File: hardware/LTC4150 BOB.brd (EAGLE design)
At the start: 15.2 x 30.5 mm, 23 parts, among them U1 LTC4150

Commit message: Final cleanup for reds
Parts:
- moved FRAME1 2.54 mm to (-22.9, -11.4)
- moved C2 0.32 mm to (4.45, 14.0)
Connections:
- net VCC renamed VIO
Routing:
- net GND: vias 7 -> 9
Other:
- board text added: "V10"
- board text added: "VIO"
- board text removed: "V02"
- board text removed: "VCC"

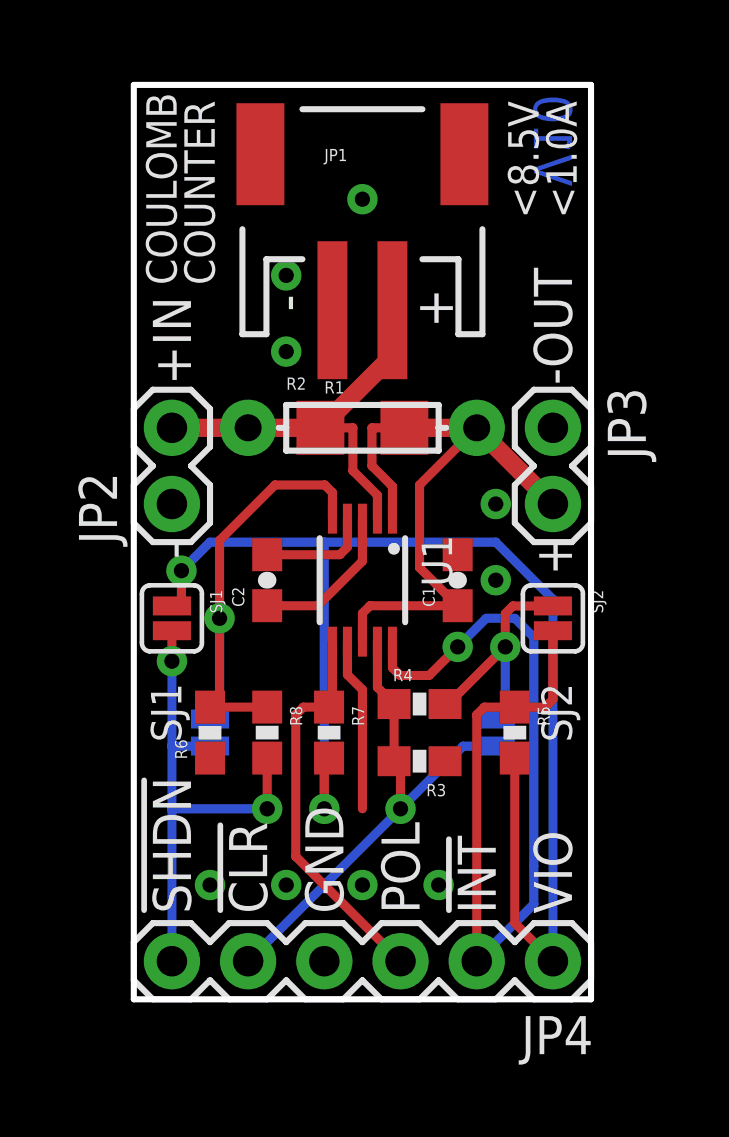
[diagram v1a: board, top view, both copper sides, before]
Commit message: fixed resistor layout for 5V operation
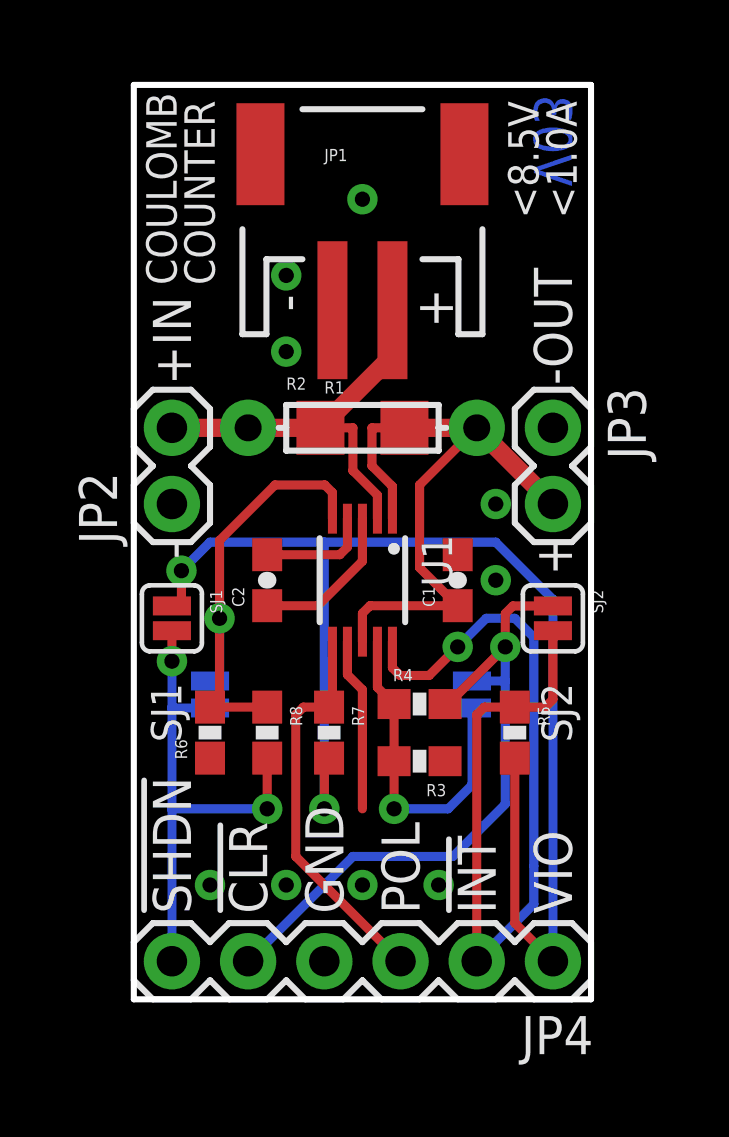
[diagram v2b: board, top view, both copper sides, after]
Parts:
- moved SJ3 1.50 mm to (11.3, 10.2)
- moved SJ4 1.27 mm to (2.54, 10.2)
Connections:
- net !CLR!: now also R4.2, SJ2.1, SJ3.2; no longer R3.2, R4.1, SJ3.1, U1.9
- net N$1: now also R3.2, R4.1, SJ3.1, U1.9; no longer R4.2, SJ2.1, SJ3.2
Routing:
- net !CLR!: track 17.1 -> 22.7 mm
- net N$1: track 8.32 -> 11.3 mm
- net N$9: track 16.6 -> 15.4 mm
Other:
- board text added: "V03"
- board text removed: "V10"
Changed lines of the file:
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@@
 <grid distance="0.05" unitdist="inch" unit="inch" style="lines" multiple="2" display="yes" altdistance="0.00625" altunitdist="inch" altunit="inch"/>
 <layers>
-<layer number="1" name="Top" color="4" fill="1" visible="yes" active="yes"/>
+<layer number="1" name="Top" color="4" fill="1" visible="no" active="yes"/>
 <layer number="2" name="Route2" color="1" fill="3" visible="no" active="no"/>
 <layer number="3" name="Route3" color="4" fill="3" visible="no" active="no"/>
@@
 <layer number="18" name="Vias" color="2" fill="1" visible="yes" active="yes"/>
 <layer number="19" name="Unrouted" color="6" fill="1" visible="yes" active="yes"/>
-<layer number="20" name="Dimension" color="15" fill="1" visible="yes" active="yes"/>
-<layer number="21" name="tPlace" color="7" fill="1" visible="yes" active="yes"/>
-<layer number="22" name="bPlace" color="7" fill="1" visible="no" active="yes"/>
+<layer number="20" name="Dimension" color="15" fill="1" visible="no" active="yes"/>
+<layer number="21" name="tPlace" color="7" fill="1" visible="no" active="yes"/>
+<layer number="22" name="bPlace" color="7" fill="1" visible="yes" active="yes"/>
 <layer number="23" name="tOrigins" color="15" fill="1" visible="no" active="yes"/>
-<layer number="24" name="bOrigins" color="15" fill="1" visible="no" active="yes"/>
+<layer number="24" name="bOrigins" color="15" fill="1" visible="yes" active="yes"/>
 <layer number="25" name="tNames" color="7" fill="1" visible="no" active="yes"/>
 <layer number="26" name="bNames" color="7" fill="1" visible="no" active="yes"/>
-<layer number="27" name="tValues" color="7" fill="1" visible="yes" active="yes"/>
+<layer number="27" name="tValues" color="7" fill="1" visible="no" active="yes"/>
 <layer number="28" name="bValues" color="7" fill="1" visible="no" active="yes"/>
 <layer number="29" name="tStop" color="7" fill="3" visible="no" active="yes"/>
@@
 <layer number="49" name="Reference" color="7" fill="1" visible="no" active="yes"/>
 <layer number="50" name="dxf" color="7" fill="1" visible="no" active="no"/>
-<layer number="51" name="tDocu" color="7" fill="1" visible="yes" active="yes"/>
+<layer number="51" name="tDocu" color="7" fill="1" visible="no" active="yes"/>
 <layer number="52" name="bDocu" color="7" fill="1" visible="no" active="yes"/>
 <layer number="53" name="tGND_GNDA" color="7" fill="9" visible="no" active="no"/>
@@
 <text x="8.255" y="25.0825" size="1.27" layer="22" ratio="15" rot="MR270">LTC4150</text>
 <text x="6.35" y="29.21" size="1.27" layer="22" ratio="15" rot="MR270">Coulomb Counter</text>
-<text x="14.605" y="30.1625" size="1.27" layer="16" ratio="20" rot="MR270">V10</text>
+<text x="14.605" y="30.1625" size="1.27" layer="16" ratio="20" rot="MR270">V03</text>
 <text x="0.635" y="20.6375" size="1.27" layer="22" ratio="15" rot="SMR90">+IN</text>
 <text x="13.335" y="20.6375" size="1.27" layer="22" ratio="15" rot="MR90">-OUT</text>
-<text x="13.335" y="7.77875" size="1.016" layer="22" ratio="15" rot="MR90">SJ3</text>
+<text x="12.54125" y="8.89" size="1.016" layer="22" ratio="15" rot="MR90">SJ3</text>
 <text x="14.605" y="8.5725" size="1.016" layer="21" ratio="15" rot="R90">SJ2</text>
 <wire x1="0" y1="0" x2="15.24" y2="0" width="0.2032" layer="20"/>
@@
 <text x="1.42875" y="23.8125" size="1.016" layer="21" font="vector" ratio="15" rot="R90">COULOMB</text>
 <text x="2.69875" y="23.8125" size="1.016" layer="21" font="vector" ratio="15" rot="R90">COUNTER</text>
-<text x="3.81" y="7.77875" size="1.016" layer="22" ratio="15" rot="MR90">SJ4</text>
+<text x="3.81" y="8.89" size="1.016" layer="22" ratio="15" rot="MR90">SJ4</text>
 <text x="10.63625" y="22.38375" size="1.27" layer="21" font="vector" ratio="15" rot="R90">+</text>
 <text x="4.445" y="23.495" size="1.27" layer="21" font="vector" ratio="15" rot="R270">-</text>
@@
 <element name="LOGO3" library="SparkFun-Aesthetics" package="SFE-LOGO-FLAME" value="LOGO-SFESK" x="8.89" y="26.67" rot="MR90"/>
 <element name="LOGO1" library="SparkFun-Aesthetics" package="OSHW-LOGO-S" value="OSHW-LOGOS" x="1.905" y="28.2575" rot="MR90"/>
-<element name="SJ3" library="mike-temp" package="SJ_2S-NO" value="" x="12.065" y="8.89" rot="MR90"/>
+<element name="SJ3" library="mike-temp" package="SJ_2S-NO" value="" x="11.27125" y="10.16" rot="MR90"/>
 <element name="SJ1" library="mike-temp" package="SJ_2S" value="" x="1.27" y="12.7" rot="R270"/>
 <element name="LOGO2" library="SparkFun-Aesthetics" package="SFE-NEW-WEB" value="LOGO-SFENW2" x="8.255" y="13.97" rot="MR90"/>
@@
 <attribute name="NAME" x="5.08" y="20.32" size="0.4064" layer="25" font="vector"/>
 </element>
-<element name="SJ4" library="mike-temp" package="SJ_2S-NO" value="" x="2.54" y="8.89" rot="MR270"/>
+<element name="SJ4" library="mike-temp" package="SJ_2S-NO" value="" x="2.54" y="10.16" rot="MR270"/>
 </elements>
 <signals>
@@
 <contactref element="SJ4" pad="1"/>
 <via x="2.8575" y="12.7" extent="1-16" drill="0.508"/>
-<wire x1="2.54" y1="9.34" x2="2.8575" y2="9.34" width="0.3048" layer="16"/>
-<wire x1="2.8575" y1="9.34" x2="2.8575" y2="12.7" width="0.3048" layer="16"/>
-</signal>
-<signal name="!CLR!">
-<contactref element="U1" pad="9"/>
-<contactref element="R3" pad="2"/>
-<contactref element="R4" pad="1"/>
-<wire x1="8.675" y1="9.8425" x2="8.675" y2="7.9375" width="0.3048" layer="1"/>
-<contactref element="SJ3" pad="1"/>
-<contactref element="JP4" pad="5"/>
-<wire x1="3.81" y1="1.27" x2="8.89" y2="6.35" width="0.3048" layer="16"/>
-<via x="8.89" y="6.35" extent="1-16" drill="0.508"/>
-<wire x1="8.89" y1="6.35" x2="8.89" y2="7.7225" width="0.3048" layer="1"/>
-<wire x1="8.89" y1="7.7225" x2="8.675" y2="7.9375" width="0.3048" layer="1"/>
-<wire x1="12.065" y1="8.44" x2="10.98" y2="8.44" width="0.3048" layer="16"/>
-<wire x1="10.98" y1="8.44" x2="8.89" y2="6.35" width="0.3048" layer="16"/>
-<wire x1="8.12" y1="11.92" x2="8.12" y2="10.3975" width="0.3048" layer="1"/>
-<wire x1="8.12" y1="10.3975" x2="8.675" y2="9.8425" width="0.3048" layer="1"/>
+<wire x1="2.54" y1="10.61" x2="2.8575" y2="10.61" width="0.3048" layer="16"/>
+<wire x1="2.8575" y1="10.61" x2="2.8575" y2="12.7" width="0.3048" layer="16"/>
 </signal>
 <signal name="!SHDN!">
@@
 <contactref element="SJ4" pad="2"/>
 <contactref element="JP4" pad="6"/>
-<wire x1="1.27" y1="8.44" x2="1.27" y2="6.35" width="0.3048" layer="16"/>
+<wire x1="1.27" y1="9.71" x2="1.27" y2="6.35" width="0.3048" layer="16"/>
 <wire x1="1.27" y1="6.35" x2="1.27" y2="1.27" width="0.3048" layer="16"/>
 <wire x1="4.445" y1="8.04" x2="4.445" y2="6.35" width="0.3048" layer="1"/>
 <via x="4.445" y="6.35" extent="1-16" drill="0.508"/>
 <wire x1="4.445" y1="6.35" x2="1.27" y2="6.35" width="0.3048" layer="16"/>
-<wire x1="1.27" y1="8.44" x2="2.54" y2="8.44" width="0.3048" layer="16"/>
-<wire x1="1.27" y1="8.44" x2="1.27" y2="11.27125" width="0.3048" layer="16"/>
+<wire x1="1.27" y1="9.71" x2="2.54" y2="9.71" width="0.3048" layer="16"/>
+<wire x1="1.27" y1="9.71" x2="1.27" y2="11.27125" width="0.3048" layer="16"/>
 </signal>
 <signal name="GND">
@@
 <wire x1="2.54" y1="15.24" x2="1.5875" y2="14.2875" width="0.3048" layer="16"/>
 </signal>
-<signal name="N$1">
+<signal name="!CLR!">
 <contactref element="R4" pad="2"/>
 <contactref element="SJ3" pad="2"/>
@@
 <wire x1="12.3825" y1="11.7475" x2="10.4775" y2="9.8425" width="0.3048" layer="1"/>
 <wire x1="10.4775" y1="9.8425" x2="10.375" y2="9.8425" width="0.3048" layer="1"/>
-<wire x1="12.065" y1="9.34" x2="12.3825" y2="9.34" width="0.3048" layer="16"/>
-<wire x1="12.3825" y1="9.34" x2="12.3825" y2="11.7475" width="0.3048" layer="16"/>
+<wire x1="11.27125" y1="10.61" x2="12.3825" y2="10.61" width="0.3048" layer="16"/>
+<wire x1="12.3825" y1="10.61" x2="12.3825" y2="11.7475" width="0.3048" layer="16"/>
+<contactref element="JP4" pad="5"/>
+<wire x1="3.81" y1="1.27" x2="7.3025" y2="4.7625" width="0.3048" layer="16"/>
+<wire x1="7.3025" y1="4.7625" x2="10.63625" y2="4.7625" width="0.3048" layer="16"/>
+<wire x1="10.63625" y1="4.7625" x2="12.3825" y2="6.50875" width="0.3048" layer="16"/>
+<wire x1="12.3825" y1="6.50875" x2="12.3825" y2="10.61" width="0.3048" layer="16"/>
+</signal>
+<signal name="N$1">
+<contactref element="R3" pad="2"/>
+<contactref element="SJ3" pad="1"/>
+<contactref element="R4" pad="1"/>
+<contactref element="U1" pad="9"/>
+<wire x1="8.12" y1="11.92" x2="8.12" y2="10.3975" width="0.3048" layer="1"/>
+<wire x1="8.12" y1="10.3975" x2="8.675" y2="9.8425" width="0.3048" layer="1"/>
+<wire x1="8.675" y1="7.9375" x2="8.675" y2="9.8425" width="0.3048" layer="1"/>
+<wire x1="8.675" y1="7.9375" x2="8.675" y2="6.35" width="0.3048" layer="1"/>
+<via x="8.675" y="6.35" extent="1-16" drill="0.508"/>
+<wire x1="8.675" y1="6.35" x2="10.4775" y2="6.35" width="0.3048" layer="16"/>
+<wire x1="11.27125" y1="9.71" x2="11.27125" y2="7.14375" width="0.3048" layer="16"/>
+<wire x1="11.27125" y1="7.14375" x2="10.4775" y2="6.35" width="0.3048" layer="16"/>
 </signal>
 </signals>
